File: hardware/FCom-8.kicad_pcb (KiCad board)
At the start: 12 copper layers, 94 x 127 mm, 86 parts, among them J101 Conn_01x04, J201 4090 USB-C, J202 9V battery, SW101 SW_DIP_x08, SW102 SW_DIP_x08, SW104 SW_DIP_x04, SW105 G19AP, SW301 Q/1/STOP, SW302 W/2/CH0, SW303 E/3/CH1, SW304 R/4/CH2, SW305 T/5/CH3, SW306 Y/6/_, SW307 U/7/-, SW308 I/8/+, SW309 O/9/=, SW310 P/0, SW311 A/!/`, SW312 S/"/CH4, SW313 D/$/CH5, SW314 F/%/CH6, SW315 G/^/CH7, SW316 H/&/{, SW317 J/*/}, SW318 K/(/[, SW319 L/)/], SW320 BKSP/DEL, SW321 SHIFT, SW322 Z/\/|, SW323 X/;/:, SW324 C/'/@, SW325 V/#/~, SW326 B/,/<, SW327 N/./>, SW328 M///?, SW329 SYM, SW330 SPC/ENT, U101 W65C02S6TPG-14, U102 AS6C1008-55PCN, U103 W65C22N6TPG-14, U104 74LS04, U105 74LS08, U106 74LS21, U201 LM1117T-5.0, U301 MCP23S17_SP, U302 NHD-0420DZ-FL-YBW, Y101 ECS-100AX-010

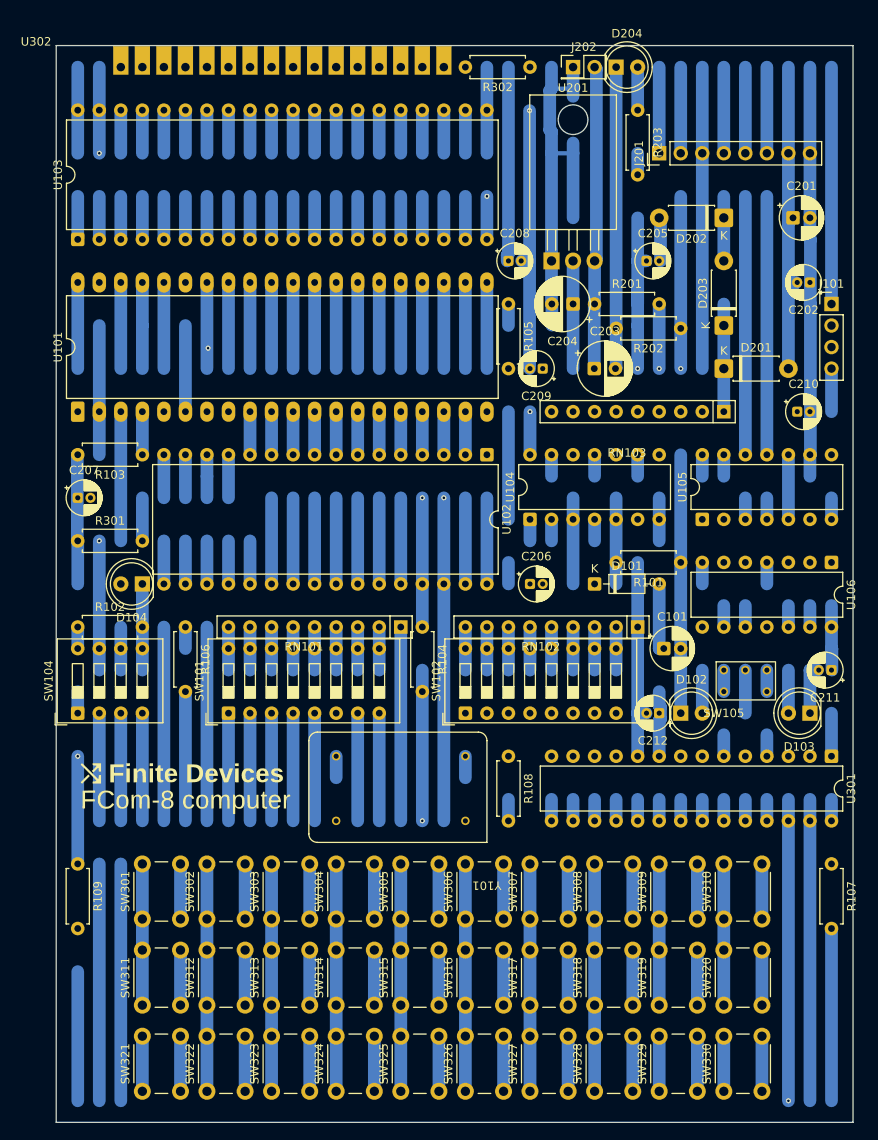
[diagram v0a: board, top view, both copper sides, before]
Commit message: Modify power circuitry to use better diode arrangement and more energy-efficient regulator
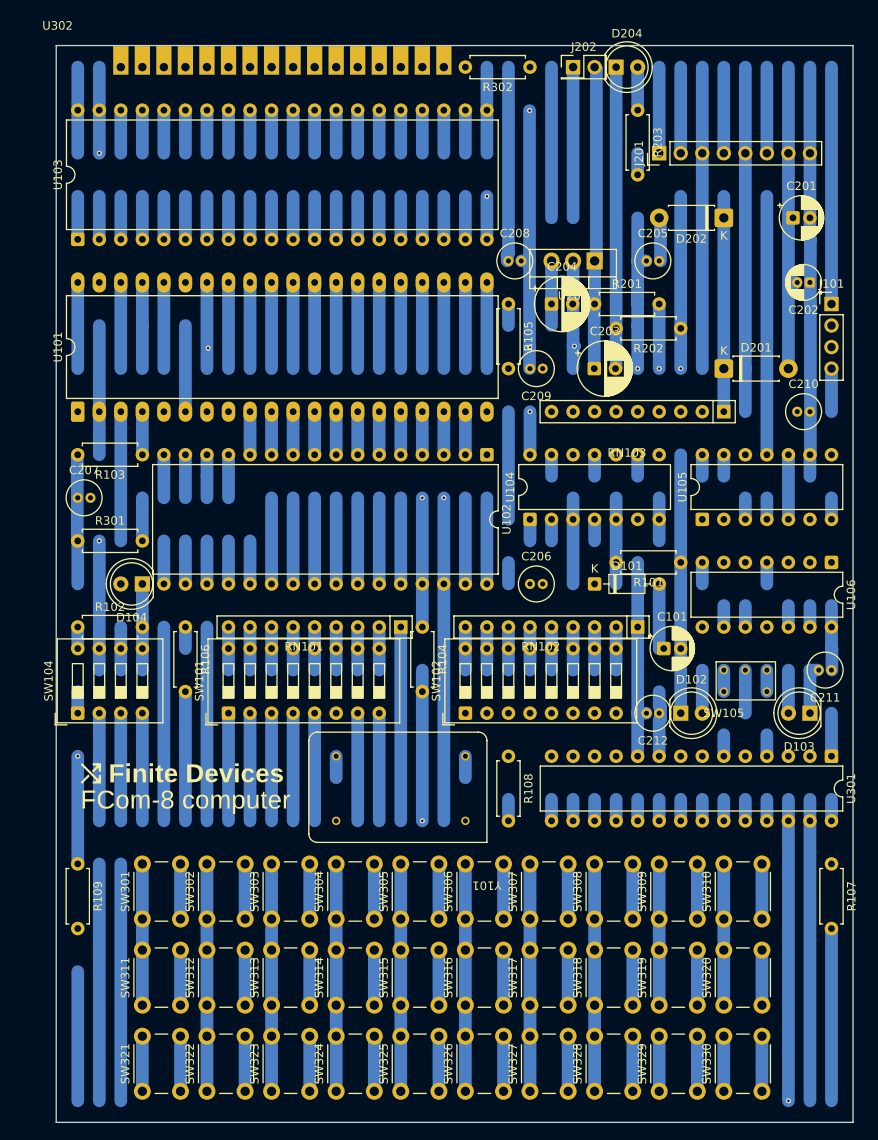
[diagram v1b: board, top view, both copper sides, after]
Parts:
- removed D203: D_Schottky, Diode_THT:D_DO-41_SOD81_P7.62mm_Horizontal
- C205, C206, C207, C208, C209, C210, C211, C212: footprint Capacitor_THT:CP_Radial_D4.0mm_P1.50mm -> Capacitor_THT:C_Radial_D4.0mm_H5.0mm_P1.50mm
- D104: value Blue LED -> Yellow LED
- R202: value 47k -> 39k
- U201: value LM1117T-5.0 -> LP2954AIT/NOPB; footprint Package_TO_SOT_THT:TO-220-3_Horizontal_TabDown -> Package_TO_SOT_THT:TO-220-3_Vertical
- U302: value NHD-0420DZ-FL-YBW -> NHD-0420DZ-NSW-BBW
- moved U201 5.08 mm to (114.3, 50.8), turned to 180 degrees
- moved C204 2.54 mm to (109.2, 55.9), turned to 0 degrees
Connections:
- D202 pad 1: Net-(D202-K) -> +5V
- U201 pad 1: GND -> Net-(J202-Pin_2)
- U201 pad 2: Net-(D202-A) -> GND
- U201 pad 3: Net-(J202-Pin_2) -> Net-(D202-A)
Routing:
- net GND: track 831.3 -> 786.3 mm, vias 3 -> 5
- net unconnected-(J201-CC1-Pad5): track 10.2 -> 40.6 mm
- net (no net): track 132.1 -> 149.9 mm
- net +5V: track 173.7 -> 186.4 mm
- net Net-(D202-K): track 7.62 -> 0.00 mm
- net Net-(D202-A): track 30.1 -> 27.6 mm
